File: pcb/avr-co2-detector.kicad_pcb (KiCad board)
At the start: 2 copper layers, 60 parts, among them J1 USB TYPE-C, J2 LCD0802, J3 AVR-ISP-10, J4 BH1.27-6-2, SW1 "Reset", SW2 "Reset", SW3 "Config", U1 ATtiny2313A-SU, U2 FT232RL, U3 004-0-0053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

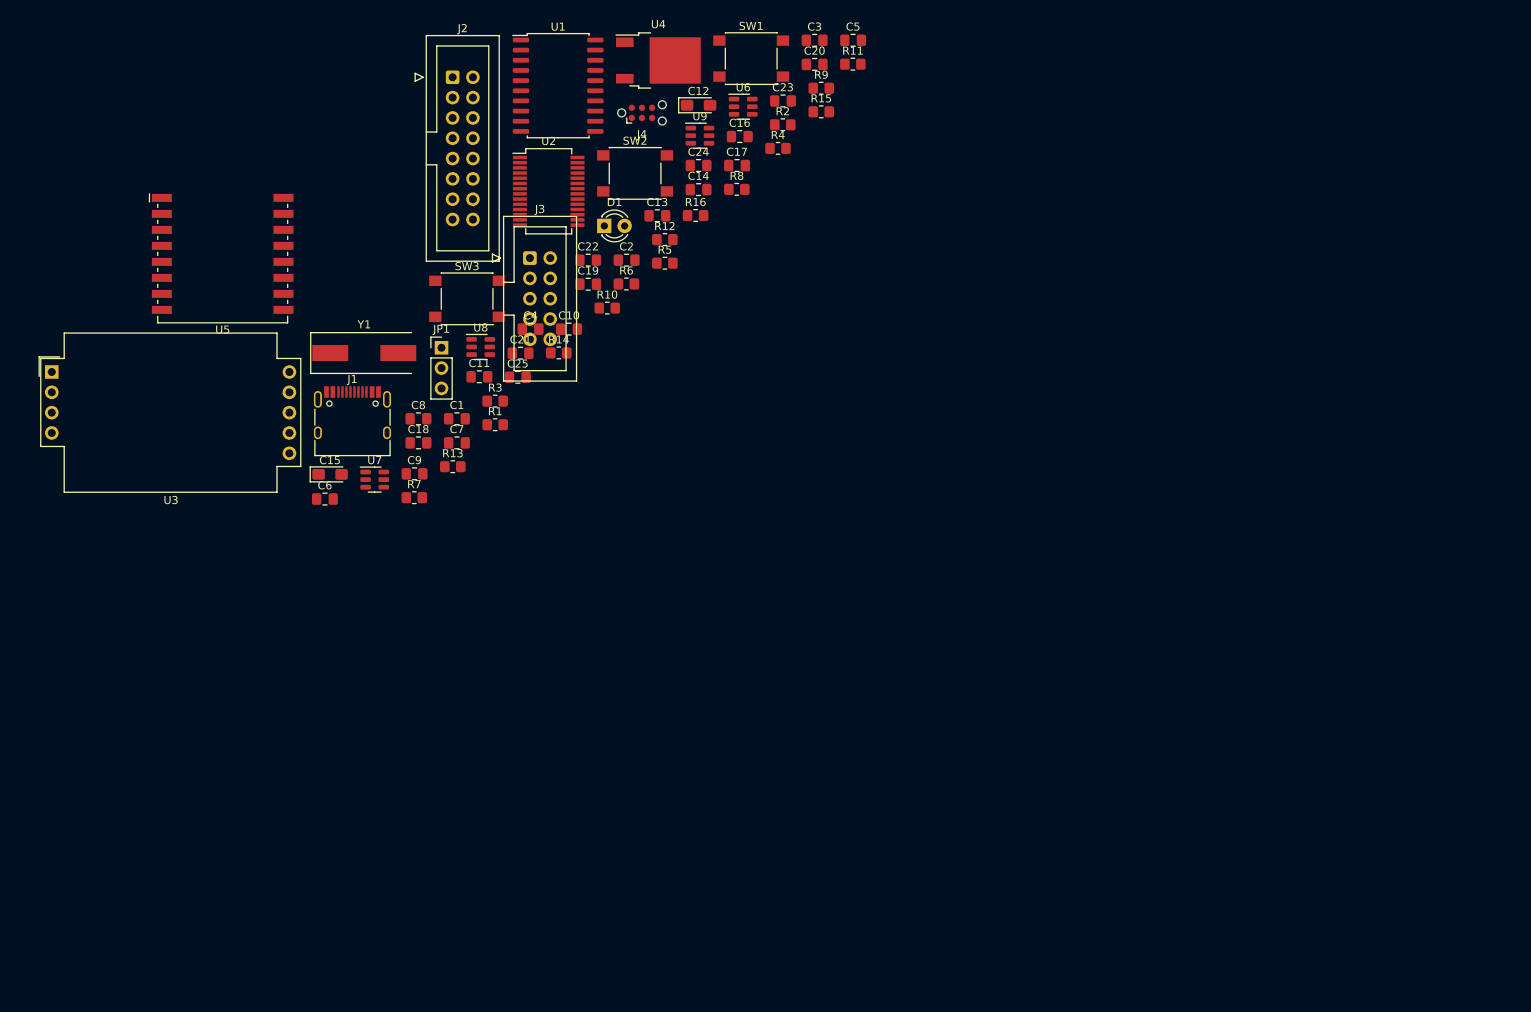
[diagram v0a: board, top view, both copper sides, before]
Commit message: Placed PCB outline, mounting holes, LCD connector, config button and LED, USB Type-C connector, SenseAir S8
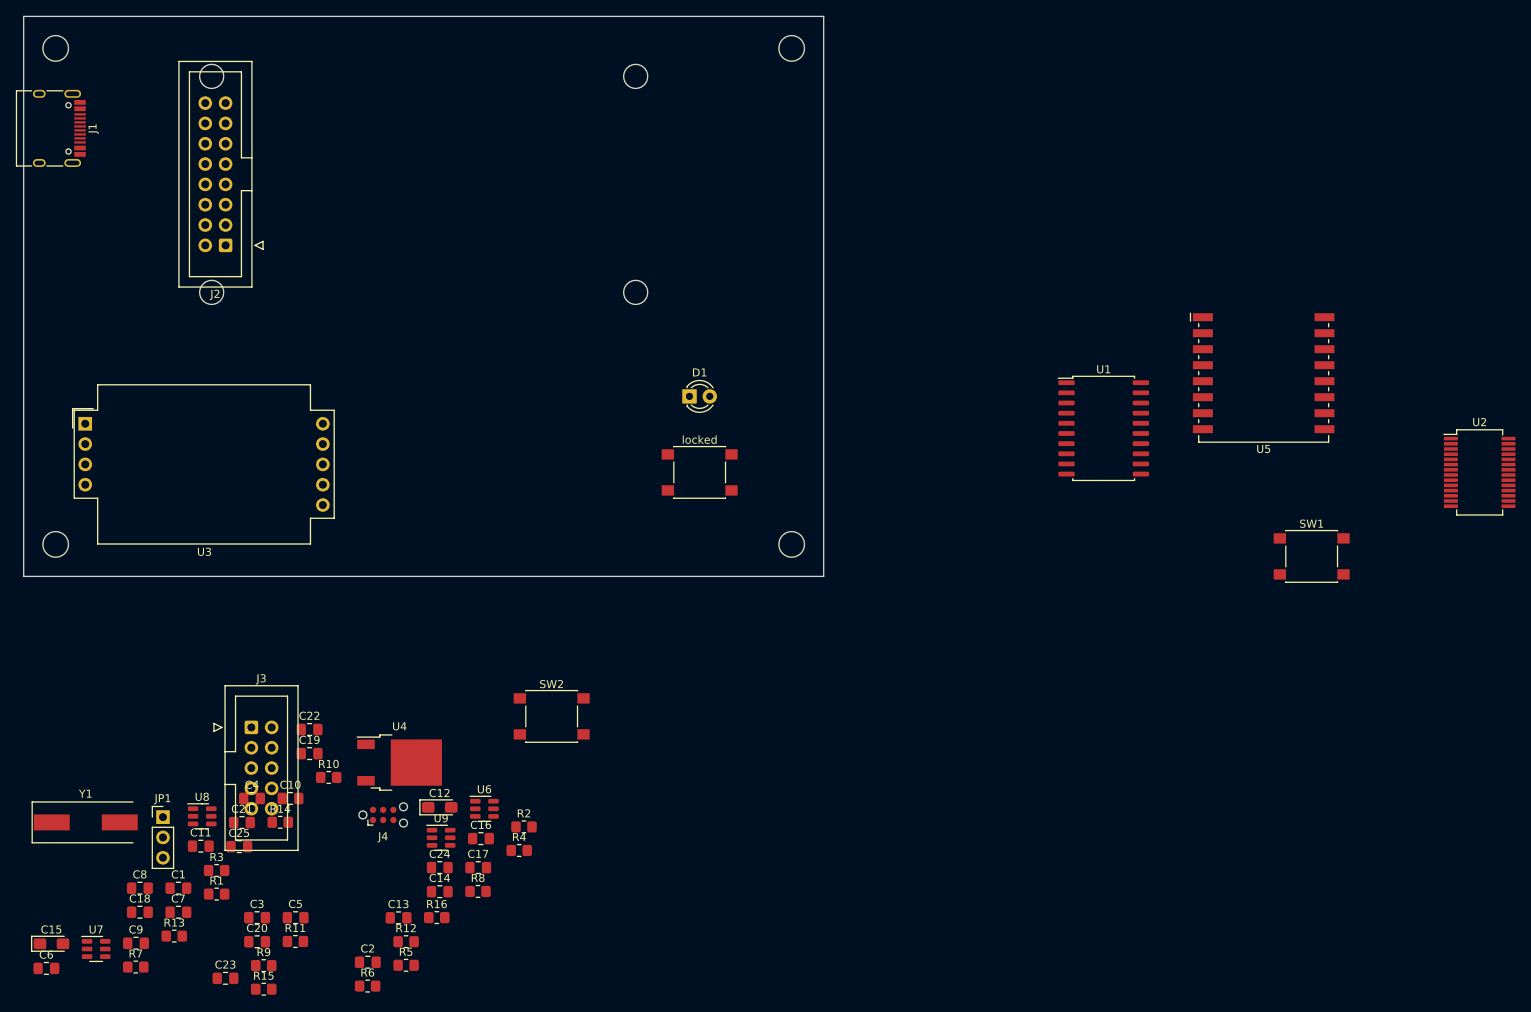
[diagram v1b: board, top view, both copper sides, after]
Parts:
- added REF**: MountingHole_3mm, MountingHole:MountingHole_3mm, F.Cu at (106.5, 98.5)
- added REF**: MountingHole_3.2mm_M3, MountingHole:MountingHole_3.2mm_M3, F.Cu at (179.0, 68.0)
- added REF**: MountingHole_3mm, MountingHole:MountingHole_3mm, F.Cu at (159.5, 98.5)
- added REF**: MountingHole_3.2mm_M3, MountingHole:MountingHole_3.2mm_M3, F.Cu at (87.0, 68.0)
- added REF**: MountingHole_3.2mm_M3, MountingHole:MountingHole_3.2mm_M3, F.Cu at (87.0, 130.0)
- added REF**: MountingHole_3mm, MountingHole:MountingHole_3mm, F.Cu at (159.5, 71.5)
- added REF**: MountingHole_3mm, MountingHole:MountingHole_3mm, F.Cu at (106.5, 71.5)
- added locked: MountingHole_3.2mm_M3, MountingHole:MountingHole_3.2mm_M3, F.Cu at (179.0, 130.0)
- locked: renamed from SW3; value "Config" -> locked
- moved U5 131.0 mm to (238.0, 106.5)
- moved C20 129.9 mm to (112.2, 179.7)
- moved C23 129.9 mm to (108.2, 184.2)
- moved C3 129.9 mm to (112.2, 176.7)
- moved C5 129.9 mm to (117.0, 176.7)
- moved R11 129.9 mm to (117.0, 179.6)
- moved R9 129.9 mm to (113.0, 182.7)
- moved R15 129.9 mm to (113.0, 185.6)
- moved U2 121.6 mm to (265.0, 121.0)
- moved SW1 93.7 mm to (244.0, 131.5)
- moved R5 93.5 mm to (130.8, 182.6)
- moved C12 93.5 mm to (135.0, 162.9)
- moved C13 93.5 mm to (129.9, 176.7)
- moved C16 93.5 mm to (140.2, 166.8)
- moved C17 93.5 mm to (139.8, 170.4)
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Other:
- board outline added: 100 x 70 mm

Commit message: Added connectors for LCD backlight
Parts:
- added J2: Backlight, Connector_PinHeader_2.54mm:PinHeader_1x01_P2.54mm_Vertical, F.Cu at (160.7, 76.5)
- added J3: Backlight, Connector_PinHeader_2.54mm:PinHeader_1x01_P2.54mm_Vertical, F.Cu at (160.7, 93.5)
- renumbered J2 to J4, J3 to J5, J4 to J6

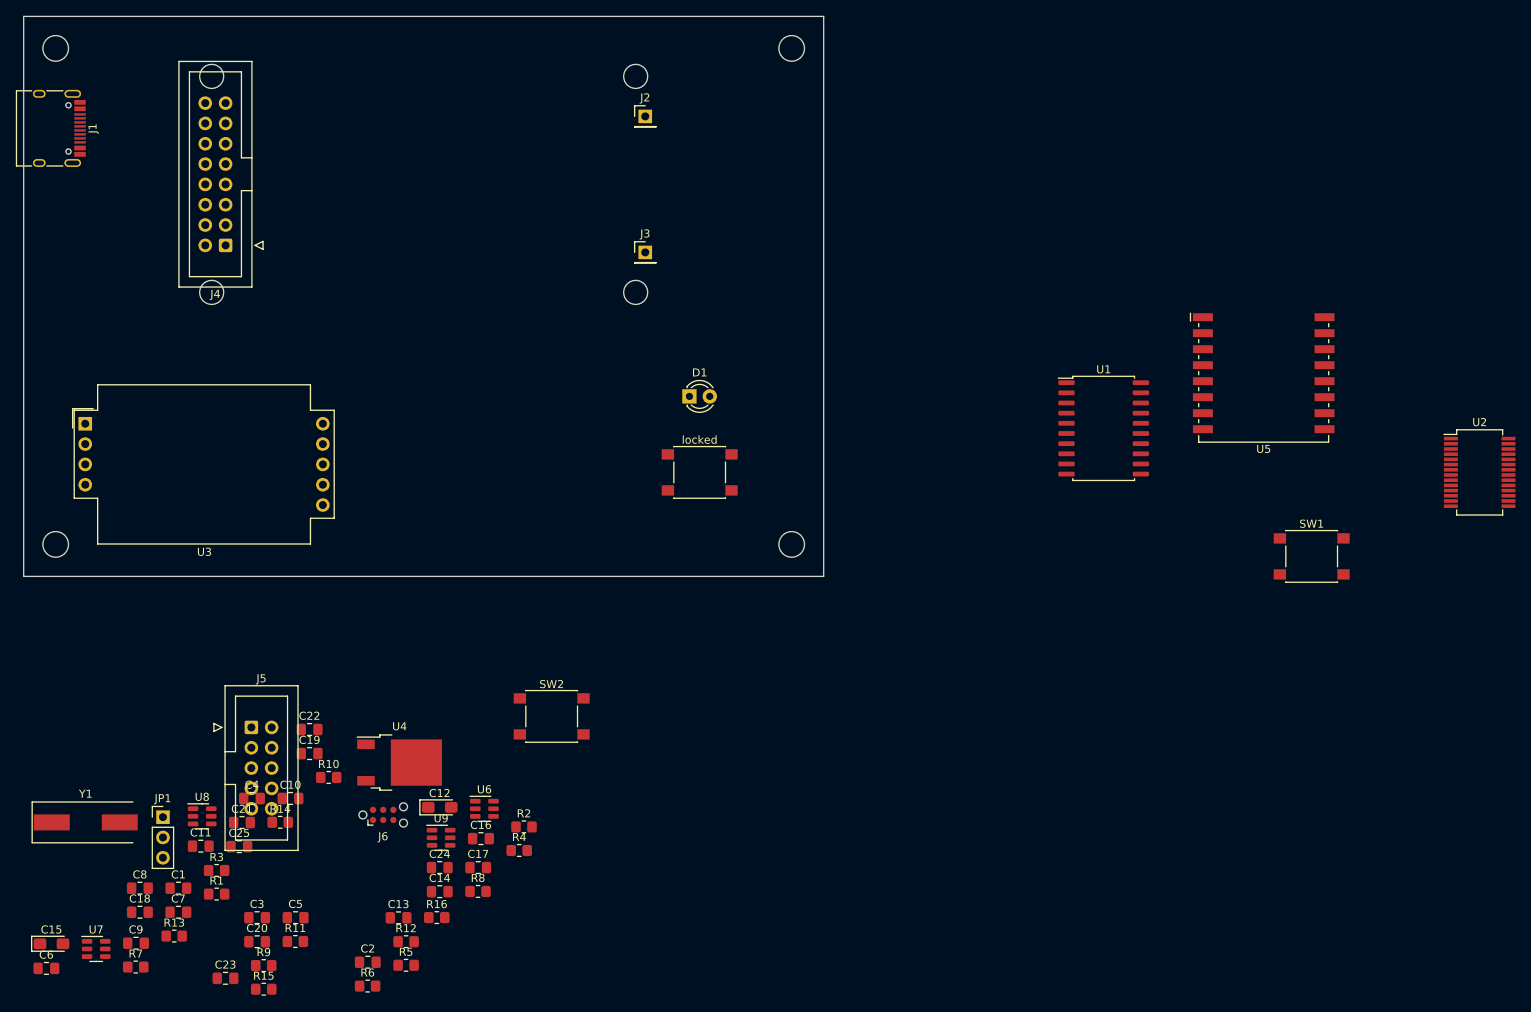
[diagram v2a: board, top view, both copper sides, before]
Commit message: Initially placed parts and routed PCB
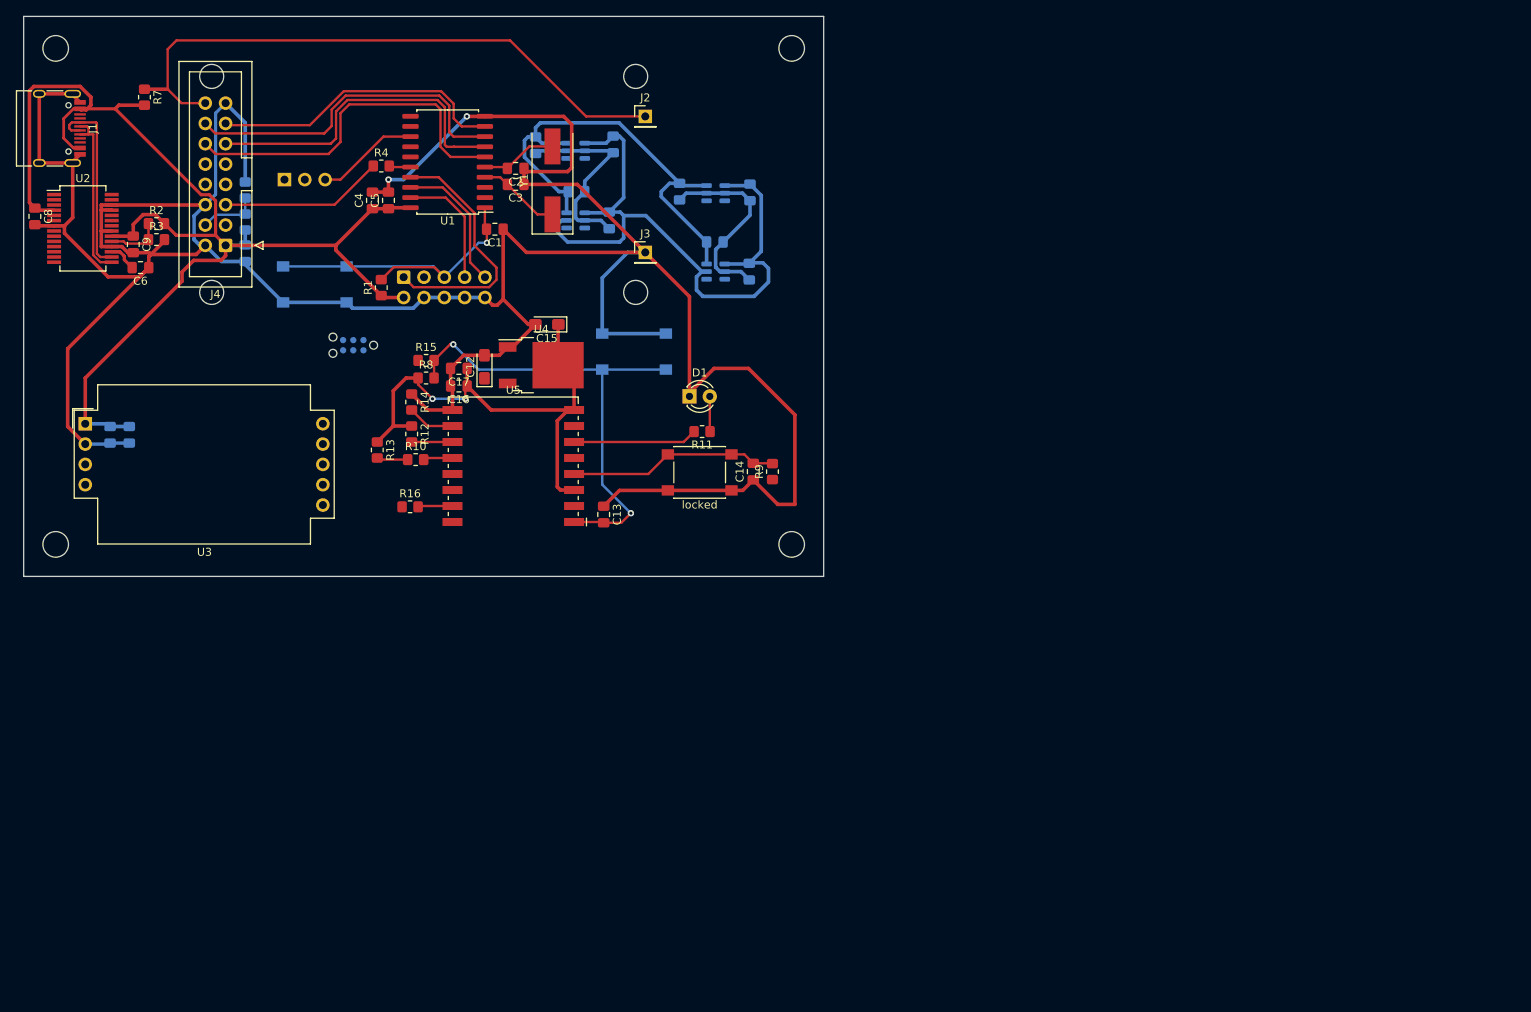
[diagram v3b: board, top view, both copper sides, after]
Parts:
- C10, C11, C18, C19, C20, C21, C22, C23, C24, C25, C7, J5, J6, JP1, R5, R6, SW1, SW2, U6, U7, U8, U9: moved to B.Cu
- moved U2 177.2 mm to (90.4, 90.5)
- moved SW1 129.2 mm to (119.4, 97.5)
- moved C18 112.7 mm to (156.7, 80.0), turned to 90 degrees
- moved U7 109.0 mm to (152.0, 89.5), turned to 180 degrees
- moved R7 108.7 mm to (98.1, 74.1), turned to -90 degrees
- moved C23 107.7 mm to (152.1, 85.9)
- moved C21 101.2 mm to (173.8, 86.0), turned to 90 degrees
- moved C2 100.9 mm to (144.5, 83.0), turned to 180 degrees
- moved U8 100.9 mm to (169.5, 86.1), turned to 180 degrees
- moved C20 100.3 mm to (156.2, 89.5), turned to 90 degrees
- moved Y1 99.2 mm to (149.1, 84.5), turned to 90 degrees
- moved C15 99.1 mm to (148.4, 102.5), turned to 180 degrees
- moved R5 99.0 mm to (110.7, 85.7), turned to 90 degrees
- moved C3 97.2 mm to (144.5, 85.0), turned to 180 degrees
- moved R6 96.7 mm to (110.7, 89.7), turned to 90 degrees
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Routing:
- net GND: track 0.00 -> 457.0 mm, vias 0 -> 2
- net +5V: track 0.00 -> 219.9 mm
- net +3.3V: track 0.00 -> 146.0 mm, vias 0 -> 2
- net /LED+: track 0.00 -> 77.4 mm
- net Net-(C13-Pad2): track 0.00 -> 60.4 mm, vias 0 -> 2
- net /DB4: track 0.00 -> 45.6 mm
- net /DB6: track 0.00 -> 42.7 mm
- net /DB5: track 0.00 -> 41.8 mm
- net Net-(C1-Pad2): track 0.00 -> 41.3 mm, vias 0 -> 1
- net /DB7: track 0.00 -> 37.2 mm
- net Net-(J5-Pad1): track 0.00 -> 31.8 mm
- net Net-(C14-Pad2): track 0.00 -> 26.3 mm
- net Net-(J1-PadA7): track 0.00 -> 23.8 mm
- net Net-(J1-PadA6): track 0.00 -> 22.4 mm
- net /E: track 0.00 -> 20.5 mm
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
